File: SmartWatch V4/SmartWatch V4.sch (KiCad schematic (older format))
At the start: 64 parts, among them J1 10118192-0001LF, J10 TestPad, J11 TestPad, J12 TestPad, J13 TestPad, J14 TestPad, J2 , J3 TestPad, J4 TestPad, J5 TestPad, J6 TestPad, J7 TestPad, J8 TestPad, J9 TestPad, Q1 FDN340P, Q2 MMBT3904, Q3 MMBT3904, Q4 FDN340P, SW1 EVQ-P7J01P, SW2 EVQ-P7J01P, U1 MAX17048, U10 TSC2003IPWR, U11 NHD-1.8-128160EF-CTXI#-T, U2 FT231XQ, U3 LP5912-3.3DRVT, U4 LP5912-2.8DRVT, U5 MCP73832-2-OT, U6 ESP32-WROOM-32, U7 NLSV4T244, U8 NLSV4T244, U9 NLSV4T244

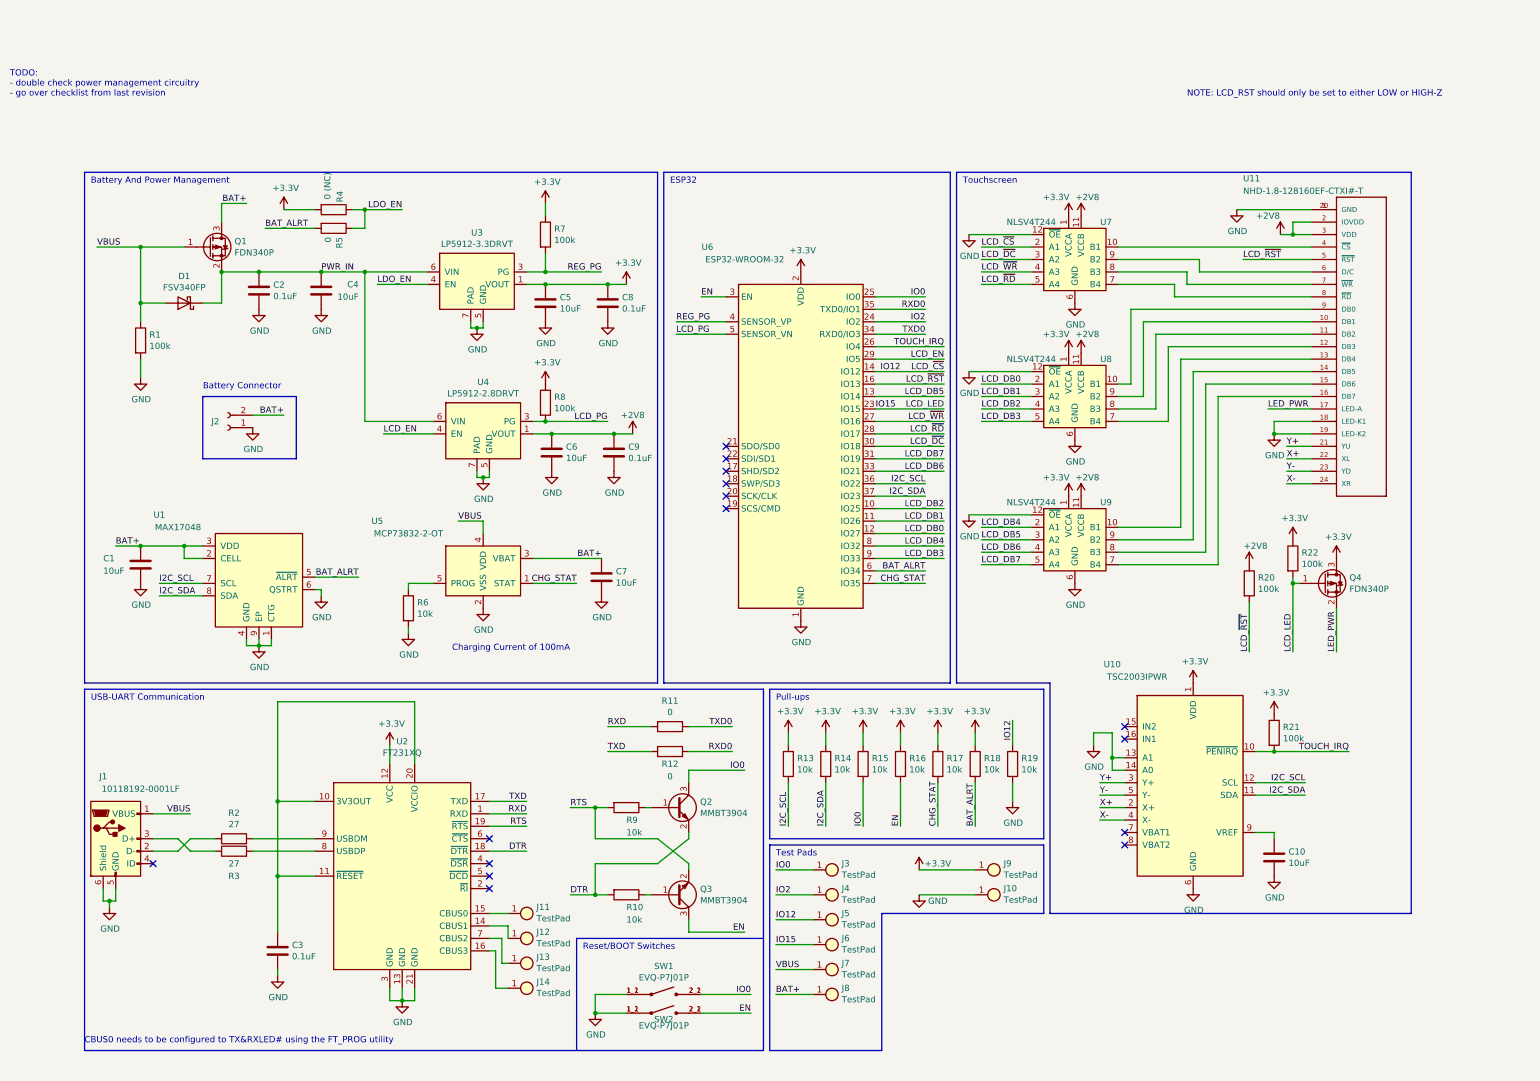
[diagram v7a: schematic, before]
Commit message: Switched to MAX17260 due to availability
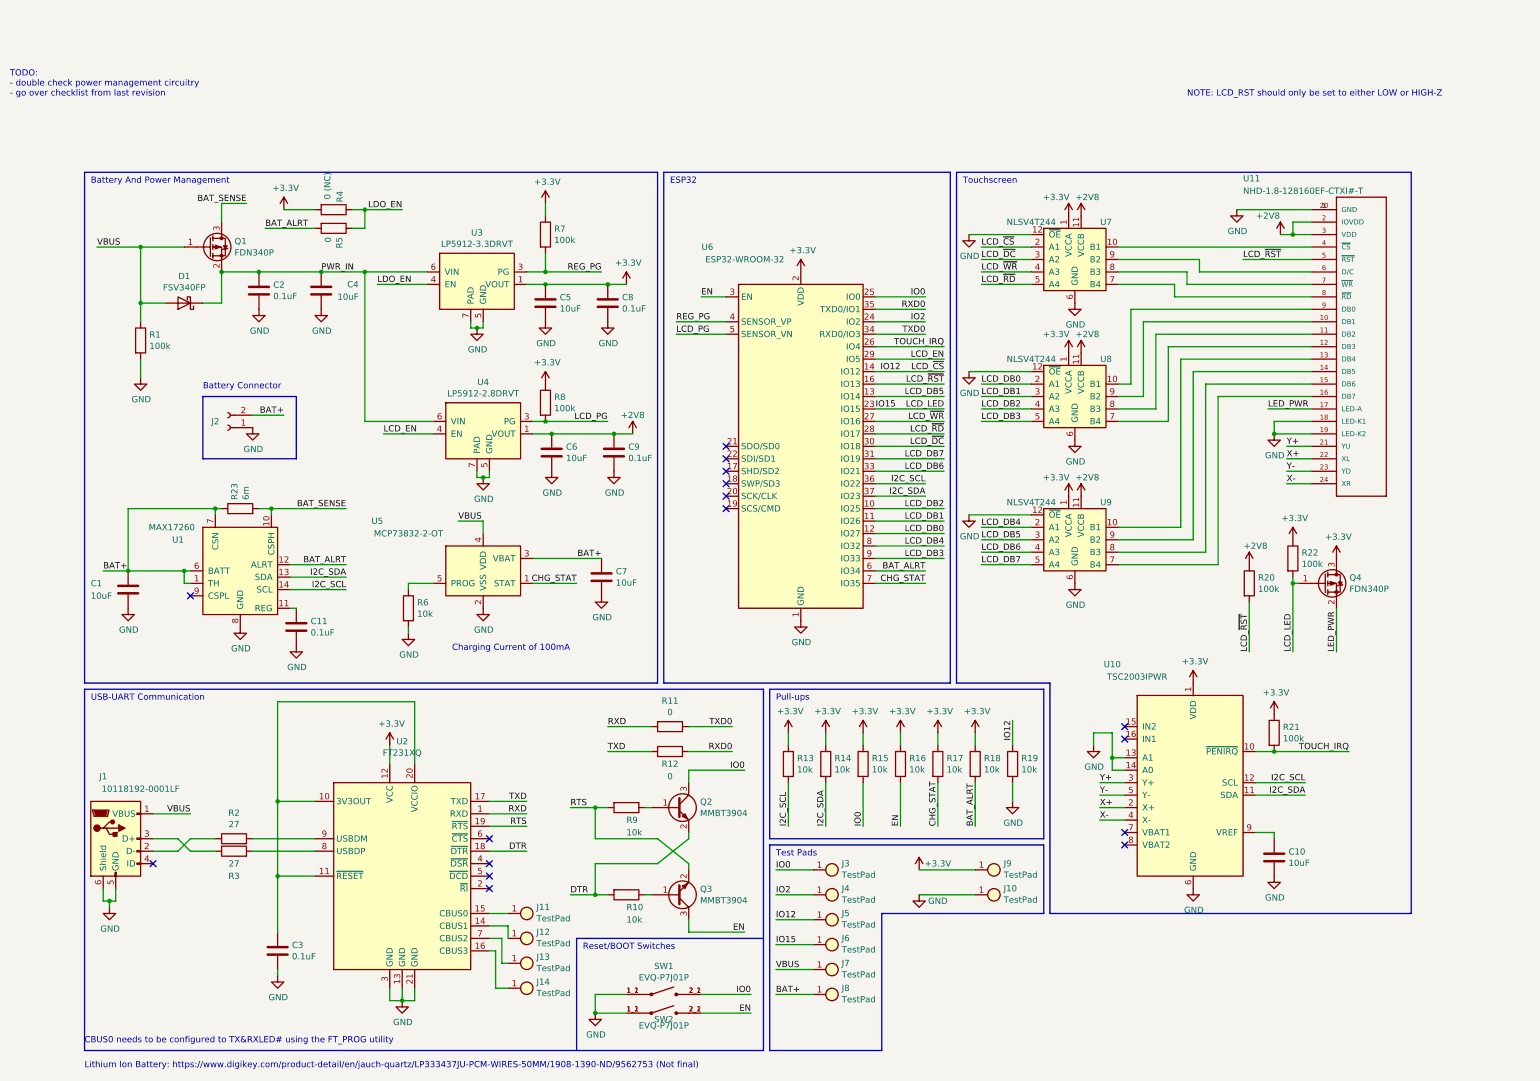
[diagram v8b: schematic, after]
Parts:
- removed U1: MAX17048, CustomFootprints:SON50P200X200X80-9N, symbol CustomParts:MAX17048
- added C11: 0.1uF, Capacitor_SMD:C_0603_1608Metric, symbol Device:C
- added R23: 6m, Resistor_SMD:R_0805_2012Metric, symbol Device:R
- added U1: MAX17260, CustomFootprints:TDFN16-EP, symbol CustomParts:MAX17260
- D1: digikey (none) -> FSV340FPCT-ND
- J1: Field6 609-4613-1-ND -> (none); digikey (none) -> 609-4613-1-ND
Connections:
- net BAT+: now also R23.1, U1.1 (TH), U1.6 (BATT), U1.7 (CSN); no longer Q1.3 (D)
- net BAT_ALRT: now also U1.12 (ALRT)
- net GND: now also C11.2, U1.8 (GND)
- net I2C_SCL: now also U1.14 (SCL)
- net I2C_SDA: now also U1.13 (SDA)
- new net: C11.1, U1.11 (REG)
- new net BAT_SENSE: Q1.3 (D), R23.2, U1.10 (CSPH)
- no-connect marks 15 -> 16
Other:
- note added: "Lithium Ion Battery: https://www.digikey.com/product-detail/en/jauch-quartz/LP333437JU-PCM-WIRES-50MM/1908-1390-ND/9562753 (Not final)\n"
- moved on the sheet: C1
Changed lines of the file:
@@
 F 4 "None" H 800 5900 50  0001 L BNN "Field4"
 F 5 "Single Port 5 Contact Horizontal Right Angle Shielded Micro B USB 2.0 Connector" H 800 5900 50  0001 L BNN "Field5"
-F 6 "609-4613-1-ND" H 800 5900 50  0001 L BNN "Field6"
+F 6 "609-4613-1-ND" H 800 5900 50  0001 L BNN "digikey"
 F 7 "10118192-0001LF" H 800 5900 50  0001 L BNN "Field7"
 F 8 "https://www.digikey.com/product-detail/en/amphenol-icc-fci/10118192-0001LF/609-4613-1-ND/2785378?utm_source=snapeda&utm_medium=aggregator&utm_campaign=symbol" H 800 5900 50  0001 L BNN "Field8"
@@
 F 2 "Diode_SMD:D_SOD-123" H 1350 1600 50  0001 C CNN
 F 3 "https://www.onsemi.com/pub/Collateral/FSV360FP-D.PDF" H 1350 1600 50  0001 C CNN
+F 4 "FSV340FPCT-ND" H 1350 1600 50  0001 C CNN "digikey"
 	1    1350 1600
 	-1   0    0    1
@@
 	1650 800  1850 800
 Text Label 1850 800  2    50   ~ 0
-BAT+
+BAT_SENSE
 Wire Wire Line
 	1650 800  1650 950
@@
 Wire Bus Line
 	5150 4650 550  4650
-Wire Wire Line
-	2400 3800 2750 3800
-Text Label 2750 3800 2    50   ~ 0
-BAT_ALRT
 Text Label 4500 3850 2    50   ~ 0
 CHG_STAT
@@
 	1    0    0    -1
 $EndComp
-Wire Wire Line
-	2450 3900 2450 3950
-Wire Wire Line
-	2400 3900 2450 3900
-$Comp
-L power:GND #PWR0142
-U 1 1 5E922E03
-P 2450 3950
-F 0 "#PWR0142" H 2450 3700 50  0001 C CNN
-F 1 "GND" H 2455 3777 50  0000 C CNN
-F 2 "" H 2450 3950 50  0001 C CNN
-F 3 "" H 2450 3950 50  0001 C CNN
-	1    2450 3950
-	1    0    0    -1
-$EndComp
 $Comp
 L power:GND #PWR0143
 U 1 1 5E91C7C2
-P 1000 3850
-F 0 "#PWR0143" H 1000 3600 50  0001 C CNN
-F 1 "GND" H 1005 3677 50  0000 C CNN
-F 2 "" H 1000 3850 50  0001 C CNN
-F 3 "" H 1000 3850 50  0001 C CNN
-	1    1000 3850
-	1    0    0    -1
-$EndComp
-Wire Wire Line
-	1000 3550 1350 3550
-Connection ~ 1000 3550
-Wire Wire Line
-	1350 3550 1500 3550
-Connection ~ 1350 3550
-Wire Wire Line
-	1350 3650 1350 3550
-Wire Wire Line
-	1500 3650 1350 3650
-Wire Wire Line
-	800  3550 1000 3550
-Wire Wire Line
-	1150 3950 1500 3950
-Wire Wire Line
-	1150 3850 1500 3850
-Text Label 1150 3850 0    50   ~ 0
-I2C_SCL
-Text Label 1150 3950 0    50   ~ 0
-I2C_SDA
-Text Label 800  3550 0    50   ~ 0
+P 900 4050
+F 0 "#PWR0143" H 900 3800 50  0001 C CNN
+F 1 "GND" H 905 3877 50  0000 C CNN
+F 2 "" H 900 4050 50  0001 C CNN
+F 3 "" H 900 4050 50  0001 C CNN
+	1    900  4050
+	1    0    0    -1
+$EndComp
+Connection ~ 900  3750
+Wire Wire Line
+	700  3750 900  3750
+Text Label 700  3750 0    50   ~ 0
 BAT+
-Wire Wire Line
-	1950 4300 1950 4350
-Wire Wire Line
-	1950 4350 2050 4350
-Connection ~ 1950 4350
-Wire Wire Line
-	2050 4350 2050 4300
-Wire Wire Line
-	1850 4350 1950 4350
-Wire Wire Line
-	1850 4300 1850 4350
-$Comp
-L power:GND #PWR0144
-U 1 1 5E8F1098
-P 1950 4350
-F 0 "#PWR0144" H 1950 4100 50  0001 C CNN
-F 1 "GND" H 1955 4177 50  0000 C CNN
-F 2 "" H 1950 4350 50  0001 C CNN
-F 3 "" H 1950 4350 50  0001 C CNN
-	1    1950 4350
-	1    0    0    -1
-$EndComp
-$Comp
-L CustomParts:MAX17048 U1
-U 1 1 5E8D870E
-P 1950 3850
-F 0 "U1" H 1150 4400 50  0000 C CNN
-F 1 "MAX17048" H 1300 4300 50  0000 C CNN
-F 2 "CustomFootprints:SON50P200X200X80-9N" H 1750 4350 50  0001 C CNN
-F 3 "https://datasheets.maximintegrated.com/en/ds/MAX17048-MAX17049.pdf" H 1750 4350 50  0001 C CNN
-F 4 "MAX17048G+T10CT-ND" H 1950 3850 50  0001 C CNN "digikey"
-	1    1950 3850
-	1    0    0    -1
-$EndComp
 $Comp
 L Device:C C1
 U 1 1 5E856FED
-P 1000 3700
-F 0 "C1" H 700 3750 50  0000 L CNN
-F 1 "10uF" H 700 3650 50  0000 L CNN
-F 2 "Capacitor_SMD:C_0603_1608Metric" H 1038 3550 50  0001 C CNN
-F 3 "~" H 1000 3700 50  0001 C CNN
-F 4 "478-10766-1-ND" H 1000 3700 50  0001 C CNN "digikey"
-	1    1000 3700
+P 900 3900
+F 0 "C1" H 600 3950 50  0000 L CNN
+F 1 "10uF" H 600 3850 50  0000 L CNN
+F 2 "Capacitor_SMD:C_0603_1608Metric" H 938 3750 50  0001 C CNN
+F 3 "~" H 900 3900 50  0001 C CNN
+F 4 "478-10766-1-ND" H 900 3900 50  0001 C CNN "digikey"
+	1    900  3900
 	1    0    0    -1
 $EndComp
@@
 Text Label 2450 1350 0    50   ~ 0
 PWR_IN
+$Comp
+L CustomParts:MAX17260 U1
+U 1 1 5EB4B3BE
+P 1800 3800
+F 0 "U1" H 1300 4100 50  0000 C CNN
+F 1 "MAX17260" H 1250 4200 50  0000 C CNN
+F 2 "CustomFootprints:TDFN16-EP" H 1150 4950 50  0001 C CNN
+F 3 "https://datasheets.maximintegrated.com/en/ds/MAX17260.pdf" H 1150 4950 50  0001 C CNN
+F 4 "175-MAX17260SEWL+TCT-ND" H 850 4850 50  0001 C CNN "digikey"
+	1    1800 3800
+	1    0    0    -1
+$EndComp
+Wire Wire Line
+	900  3750 1350 3750
+Wire Wire Line
+	1400 3850 1350 3850
+Wire Wire Line
+	1350 3850 1350 3750
+Connection ~ 1350 3750
+Wire Wire Line
+	1350 3750 1400 3750
+$Comp
+L Device:R R23
+U 1 1 5EBB9EAC
+P 1800 3250
+F 0 "R23" H 1870 3296 50  0000 L CNN
+F 1 "6m" H 1870 3205 50  0000 L CNN
+F 2 "Resistor_SMD:R_0805_2012Metric" V 1730 3250 50  0001 C CNN
+F 3 "https://d1d2qsbl8m0m72.cloudfront.net/en/products/databook/datasheet/passive/resistor/chip_resistor/pmr-e.pdf" H 1800 3250 50  0001 C CNN
+F 4 "RHM.006AKCT-ND" H 1800 3250 50  0001 C CNN "digikey"
+	1    1800 3250
+	0    -1   -1   0
+$EndComp
+Wire Wire Line
+	1600 3300 1600 3250
+Wire Wire Line
+	1600 3250 1650 3250
+Wire Wire Line
+	1600 3250 900  3250
+Wire Wire Line
+	900  3250 900  3750
+Connection ~ 1600 3250
+Wire Wire Line
+	1950 3250 2050 3250
+Wire Wire Line
+	2050 3250 2050 3300
+Connection ~ 2050 3250
+Text Label 2650 3250 2    50   ~ 0
+BAT_SENSE
+Wire Wire Line
+	2050 3250 2650 3250
+Text Label 2650 3700 2    50   ~ 0
+BAT_ALRT
+Wire Wire Line
+	2200 3700 2650 3700
+Text Label 2650 3800 2    50   ~ 0
+I2C_SDA
+Text Label 2650 3900 2    50   ~ 0
+I2C_SCL
+Wire Wire Line
+	2200 3800 2650 3800
+Wire Wire Line
+	2200 3900 2650 3900
+$Comp
+L power:GND #PWR01
+U 1 1 5EE9C540
+P 1800 4200
+F 0 "#PWR01" H 1800 3950 50  0001 C CNN
+F 1 "GND" H 1805 4027 50  0000 C CNN
+F 2 "" H 1800 4200 50  0001 C CNN
+F 3 "" H 1800 4200 50  0001 C CNN
+	1    1800 4200
+	1    0    0    -1
+$EndComp
+$Comp
+L Device:C C11
+U 1 1 5EE9CCD7
+P 2250 4200
+F 0 "C11" H 2365 4246 50  0000 L CNN
+F 1 "0.1uF" H 2365 4155 50  0000 L CNN
+F 2 "Capacitor_SMD:C_0603_1608Metric" H 2288 4050 50  0001 C CNN
+F 3 "~" H 2250 4200 50  0001 C CNN
+F 4 "1276-1006-1-ND" H 2250 4200 50  0001 C CNN "digikey"
+	1    2250 4200
+	1    0    0    -1
+$EndComp
+Wire Wire Line
+	2200 4050 2250 4050
+$Comp
+L power:GND #PWR02
+U 1 1 5EEB600A
+P 2250 4350
+F 0 "#PWR02" H 2250 4100 50  0001 C CNN
+F 1 "GND" H 2255 4177 50  0000 C CNN
+F 2 "" H 2250 4350 50  0001 C CNN
+F 3 "" H 2250 4350 50  0001 C CNN
+	1    2250 4350
+	1    0    0    -1
+$EndComp
+NoConn ~ 1400 3950
+Text Notes 550  7750 0    50   ~ 0
+Lithium Ion Battery: https://www.digikey.com/product-detail/en/jauch-quartz/LP333437JU-PCM-WIRES-50MM/1908-1390-ND/9562753 (Not final)\n
 $EndSCHEMATC
